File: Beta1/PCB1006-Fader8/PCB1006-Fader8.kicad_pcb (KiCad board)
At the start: 2 copper layers, 155 x 62 mm, 46 parts, among them U1000 MCP3008T-I/SL

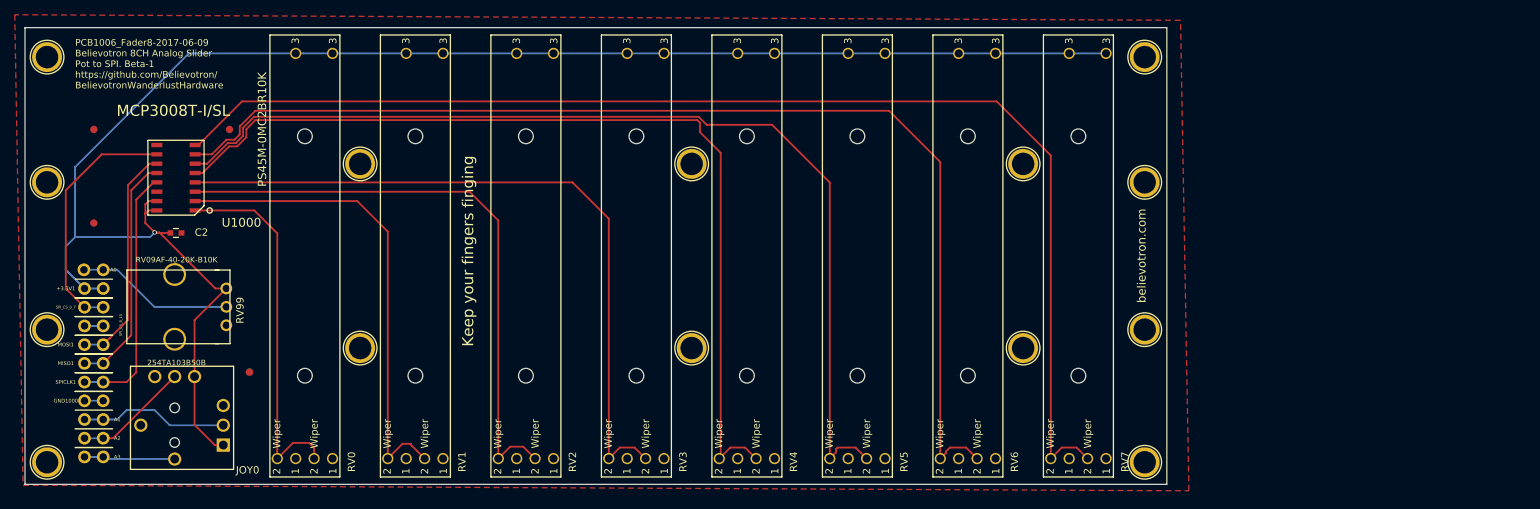
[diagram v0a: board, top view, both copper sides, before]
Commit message: Added USB-K connector
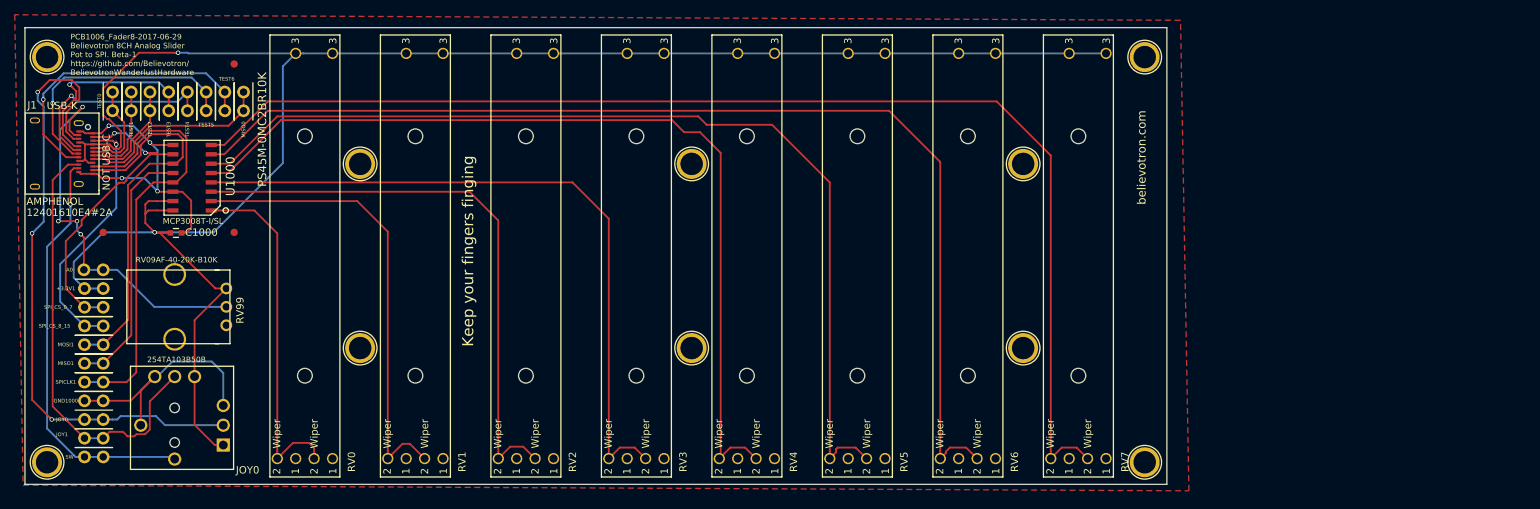
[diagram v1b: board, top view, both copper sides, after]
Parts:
- removed the REF** at (152.0, -41.0)
- removed the REF** at (3.00, -21.0)
- removed the REF** at (3.00, -41.0)
- removed the REF** at (30.5, -15.2) (x2)
- removed the REF** at (152.0, -21.0)
- added J1: USB-K, Liberry:USB-K_12401610E4_2A, F.Cu at (8.55, -44.9)
- added MISO0: CONN_01X01, Liberry:TH_0.1_1x2_Jumper, F.Cu at (29.7, -50.7)
- added TEST0: CONN_01X01, Liberry:TH_0.1_1x2_Jumper, F.Cu at (11.9, -50.7)
- added TEST1: CONN_01X01, Liberry:TH_0.1_1x2_Jumper, F.Cu at (14.4, -50.7)
- added TEST2: CONN_01X01, Liberry:TH_0.1_1x2_Jumper, F.Cu at (17.0, -50.7)
- added TEST3: CONN_01X01, Liberry:TH_0.1_1x2_Jumper, F.Cu at (19.5, -50.7)
- added TEST4: CONN_01X01, Liberry:TH_0.1_1x2_Jumper, F.Cu at (22.1, -50.7)
- added TEST5: CONN_01X01, Liberry:TH_0.1_1x2_Jumper, F.Cu at (24.6, -50.7)
- added TEST6: CONN_01X01, Liberry:TH_0.1_1x2_Jumper, F.Cu at (27.1, -50.7)
- moved REF** 21.0 mm to (28.4, -57.1)
- moved REF** 14.0 mm to (28.4, -34.2)
- moved U1000 2.18 mm to (22.7, -41.6)
- moved REF** 1.80 mm to (10.6, -34.2)
- renumbered C2 to C1000
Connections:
- net Net-(A1-Pad1) renamed /JOY0
- net Net-(A2-Pad1) renamed /JOY1
- net Net-(A3-Pad1) renamed /JOY_SW
- SPI_CS_8_15 pad 1: /CS_LED_8_15 -> /CS_R8_15
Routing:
- net GND: track 2.54 -> 77.1 mm, vias 0 -> 4
- net /JOY0: track 20.2 -> 86.1 mm, vias 0 -> 3
- net /JOY_SW: track 12.4 -> 56.5 mm, vias 0 -> 1
- net /JOY1: track 15.7 -> 59.7 mm
- net /TEST6: track 0.00 -> 41.0 mm, vias 0 -> 1
- net +3V3: track 226.2 -> 266.6 mm, vias 1 -> 2
- net /TEST5: track 0.00 -> 35.6 mm, vias 0 -> 1
- net /CS_R8_15: track 0.00 -> 35.5 mm, vias 0 -> 1
- net /VOLUME: track 21.4 -> 53.2 mm, vias 0 -> 4
- net /TEST4: track 0.00 -> 28.7 mm, vias 0 -> 1
- net /TEST3: track 0.00 -> 27.4 mm, vias 0 -> 1
- net Net-(J1-PadA8): track 0.00 -> 26.9 mm
- net /SPICLK: track 34.8 -> 59.9 mm
- net /MOSI: track 30.7 -> 52.4 mm
- net /TEST2: track 0.00 -> 14.9 mm
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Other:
- board text added: "JOY0"
- board text added: "JOY1"
- board text added: "PCB1006_Fader8-2017-06-29 Believotron 8CH Analog Slider Pot to SPI. Beta-1 https://github.com/Believotron/ BelievotronWanderlustHardware"
- board text added: "SW"
- board text removed: "0.1 uF"
- board text removed: "PCB1006_Fader8-2017-06-09 Believotron 8CH Analog Slider Pot to SPI. Beta-1 https://github.com/Believotron/ BelievotronWanderlustHardware"

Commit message: PCB1006 ready for fab
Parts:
- moved REF** 14.0 mm to (166.0, -4.00)
- moved REF** 14.0 mm to (166.0, -58.0)
- moved RV7 14.0 mm to (157.0, -31.0)
- moved REF** 13.0 mm to (148.5, -18.5)
- moved REF** 13.0 mm to (148.5, -43.5)
- moved RV6 12.0 mm to (140.0, -31.0)
- moved RV5 10.0 mm to (123.0, -31.0)
- moved RV4 8.00 mm to (106.0, -31.0)
- moved REF** 7.00 mm to (97.5, -18.5)
- moved REF** 7.00 mm to (97.5, -43.5)
- moved RV3 6.00 mm to (89.0, -31.0)
- moved RV2 4.00 mm to (72.0, -31.0)
- moved RV1 2.00 mm to (55.0, -31.0)
- moved REF** 1.00 mm to (3.00, -4.00)
- moved REF** 1.00 mm to (46.5, -18.5)
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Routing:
- net +3V3: track 266.6 -> 382.6 mm
- net /P7: track 166.8 -> 183.1 mm
- net /P5: track 134.3 -> 149.4 mm
- net /P6: track 150.9 -> 165.9 mm
- net /P4: track 121.8 -> 131.9 mm
- net /P3: track 94.8 -> 101.8 mm
- net /P2: track 79.2 -> 84.3 mm
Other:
- board size 155 x 62 mm -> 169 x 62 mm
- board text added: "PCB1006_Fader8-2017-07-11 Believotron 8CH Analog Slider Pot to SPI. Beta-1 https://github.com/Believotron/ BelievotronWanderlustHardware"
- board text added: "PS45M-0MC2BR10K x8"
- board text removed: "PCB1006_Fader8-2017-06-29 Believotron 8CH Analog Slider Pot to SPI. Beta-1 https://github.com/Believotron/ BelievotronWanderlustHardware"
- board text removed: "PS45M-0MC2BR10K"

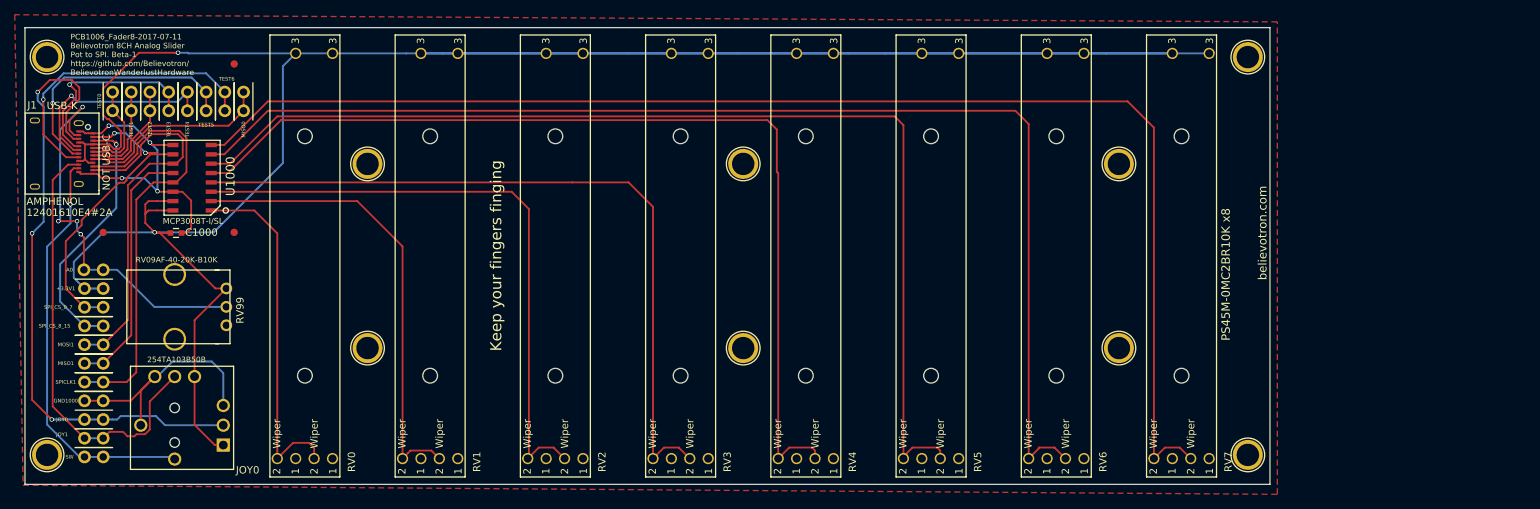
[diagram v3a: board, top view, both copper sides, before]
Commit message: Changed joystick to alps, moved, routed.
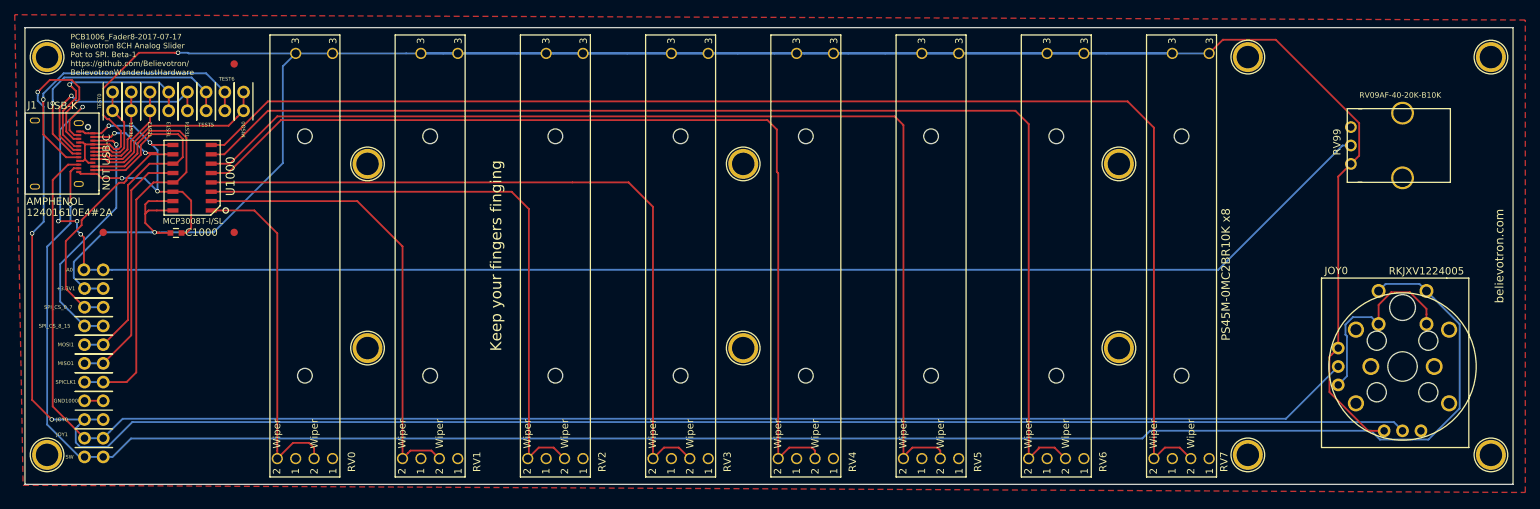
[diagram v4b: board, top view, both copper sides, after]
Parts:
- added REF**: 1pin, Connect:1pin, F.Cu at (199.0, -4.00)
- added REF**: 1pin, Connect:1pin, F.Cu at (199.0, -58.0)
- JOY0: value XYJOY -> XYJOY_Alps; footprint Liberry:XY_JOY_254TA103B50B -> Liberry:JOY_ALPS_RKJXV1224005
- moved RV99 168.1 mm to (187.0, -46.0), turned to 270 degrees
- moved JOY0 166.9 mm to (187.0, -16.0)
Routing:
- net /JOY_SW: track 56.2 -> 259.3 mm
- net /JOY0: track 86.1 -> 255.0 mm
- net /VOLUME: track 53.2 -> 210.8 mm
- net /JOY1: track 59.7 -> 215.5 mm
- net +3V3: track 382.6 -> 418.6 mm
- net GND: track 77.1 -> 73.1 mm
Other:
- board size 169 x 62 mm -> 202 x 62 mm
- board text added: "PCB1006_Fader8-2017-07-17 Believotron 8CH Analog Slider Pot to SPI. Beta-1 https://github.com/Believotron/ BelievotronWanderlustHardware"
- board text added: "RKJXV1224005"
- board text removed: "254TA103B50B"
- board text removed: "PCB1006_Fader8-2017-07-11 Believotron 8CH Analog Slider Pot to SPI. Beta-1 https://github.com/Believotron/ BelievotronWanderlustHardware"
